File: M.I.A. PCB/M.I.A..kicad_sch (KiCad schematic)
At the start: 41 parts, among them J1 USB_C_Receptacle_USB2.0_16P, SW1 SW_Push, SW2 SW_Push, U1 W25Q128JVS, U2 RP2350B-QFN80, Y1 ABM8-272-T3

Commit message: Finished Layout other than gps, extra connectors, and ignition lines
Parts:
- C14, C15, C16, C3: footprint Capacitor_SMD:C_0603_1608Metric -> Capacitor_SMD:C_0805_2012Metric
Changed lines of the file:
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@@
 			)
 		)
-		(property "Footprint" "Capacitor_SMD:C_0603_1608Metric"
+		(property "Footprint" "Capacitor_SMD:C_0805_2012Metric"
 			(at 96.2152 22.86 0)
 			(effects
@@
 			)
 		)
-		(property "Footprint" "Capacitor_SMD:C_0603_1608Metric"
+		(property "Footprint" "Capacitor_SMD:C_0805_2012Metric"
 			(at 30.1752 46.99 0)
 			(effects
@@
 			)
 		)
-		(property "Footprint" "Capacitor_SMD:C_0603_1608Metric"
+		(property "Footprint" "Capacitor_SMD:C_0805_2012Metric"
 			(at 21.2852 46.99 0)
 			(effects
@@
 			)
 		)
-		(property "Footprint" "Capacitor_SMD:C_0603_1608Metric"
+		(property "Footprint" "Capacitor_SMD:C_0805_2012Metric"
 			(at 50.4952 30.48 0)
 			(effects

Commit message: Worked More on Layout/Wiring
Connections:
- net PWM1: now also U2.57 (GPIO46_ADC6)
- net PWM2: now also U2.58 (GPIO47_ADC7)
- net PWM3: now also U2.56 (GPIO45_ADC5)
- net PWM4: now also U2.55 (GPIO44_ADC4)
- net PWM5: now also U2.54 (GPIO43_ADC3)
- net PWM6: now also U2.53 (GPIO42_ADC2)
- net PWM7: now also U2.52 (GPIO41_ADC1)
- net PWM8: now also U2.49 (GPIO40_ADC0)
- net SD_ChipDetect: now also U2.44 (GPIO35)
- net SD_ChipSelect: now also U2.46 (GPIO37)
- net SPI_MISO_SD: now also U2.45 (GPIO36)
- net SPI_MOSI_SD: now also U2.48 (GPIO39)
- net SPI_SCK_SD: now also U2.47 (GPIO38)
- net IGN_4: now reaches U2.39 (GPIO31)
- net IGN_3: now reaches U2.40 (GPIO32)
- net IGN_2: now reaches U2.42 (GPIO33)
- net IGN_1: now reaches U2.43 (GPIO34)

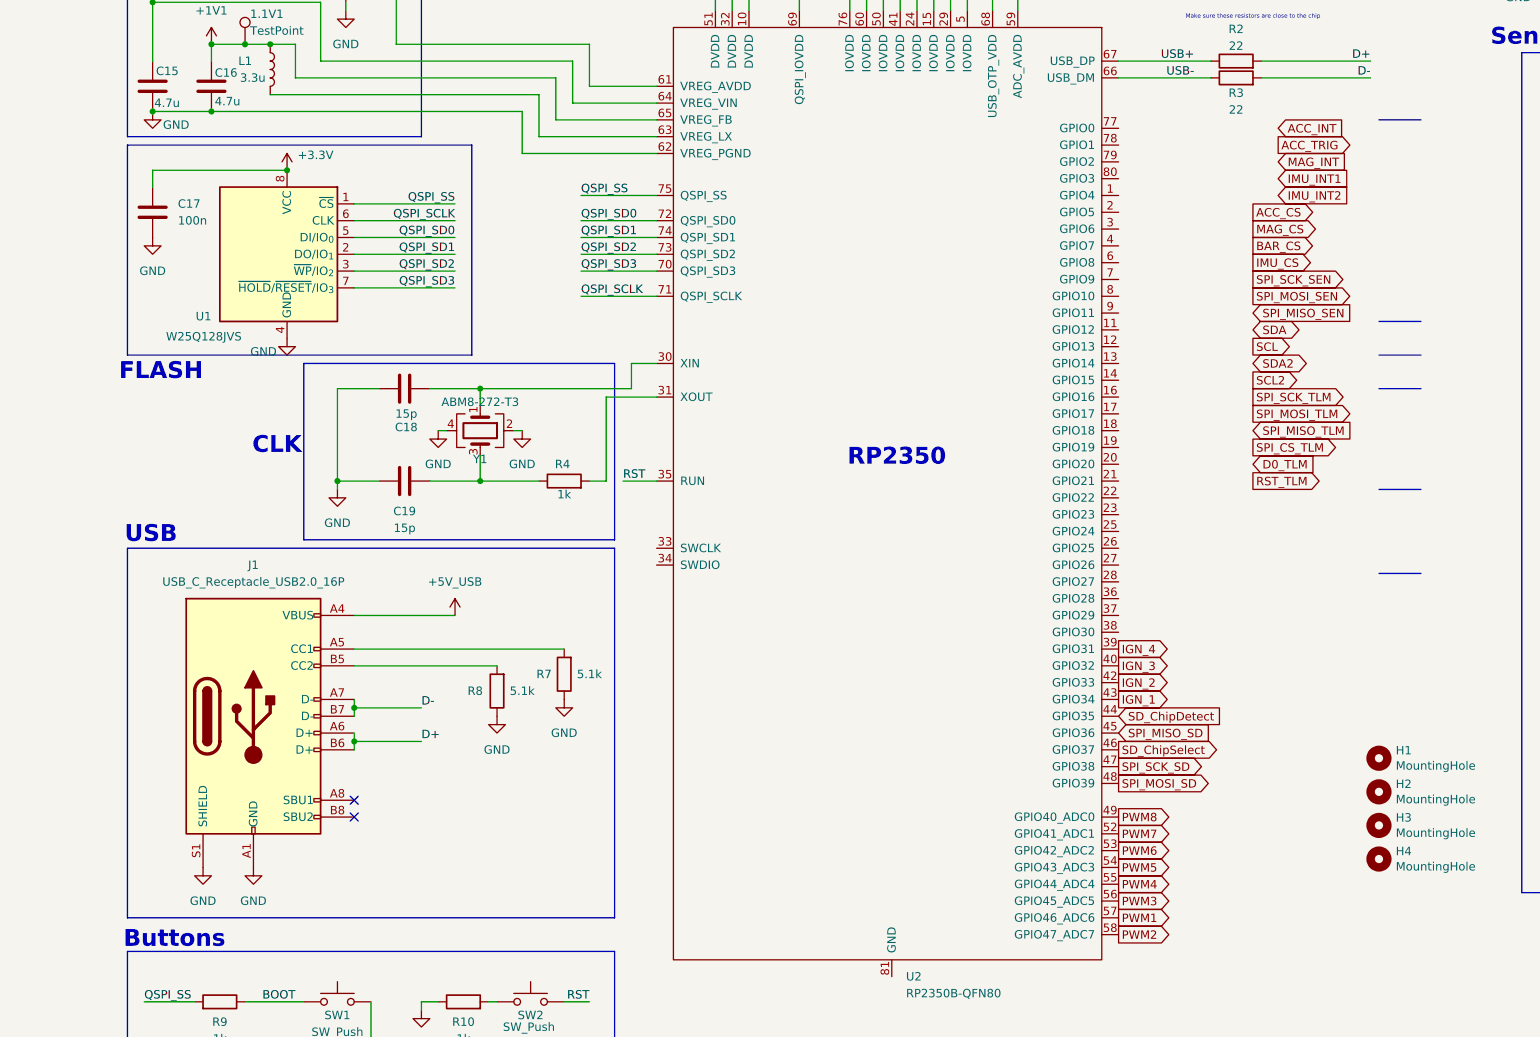
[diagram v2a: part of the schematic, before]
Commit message: Wired Sensors
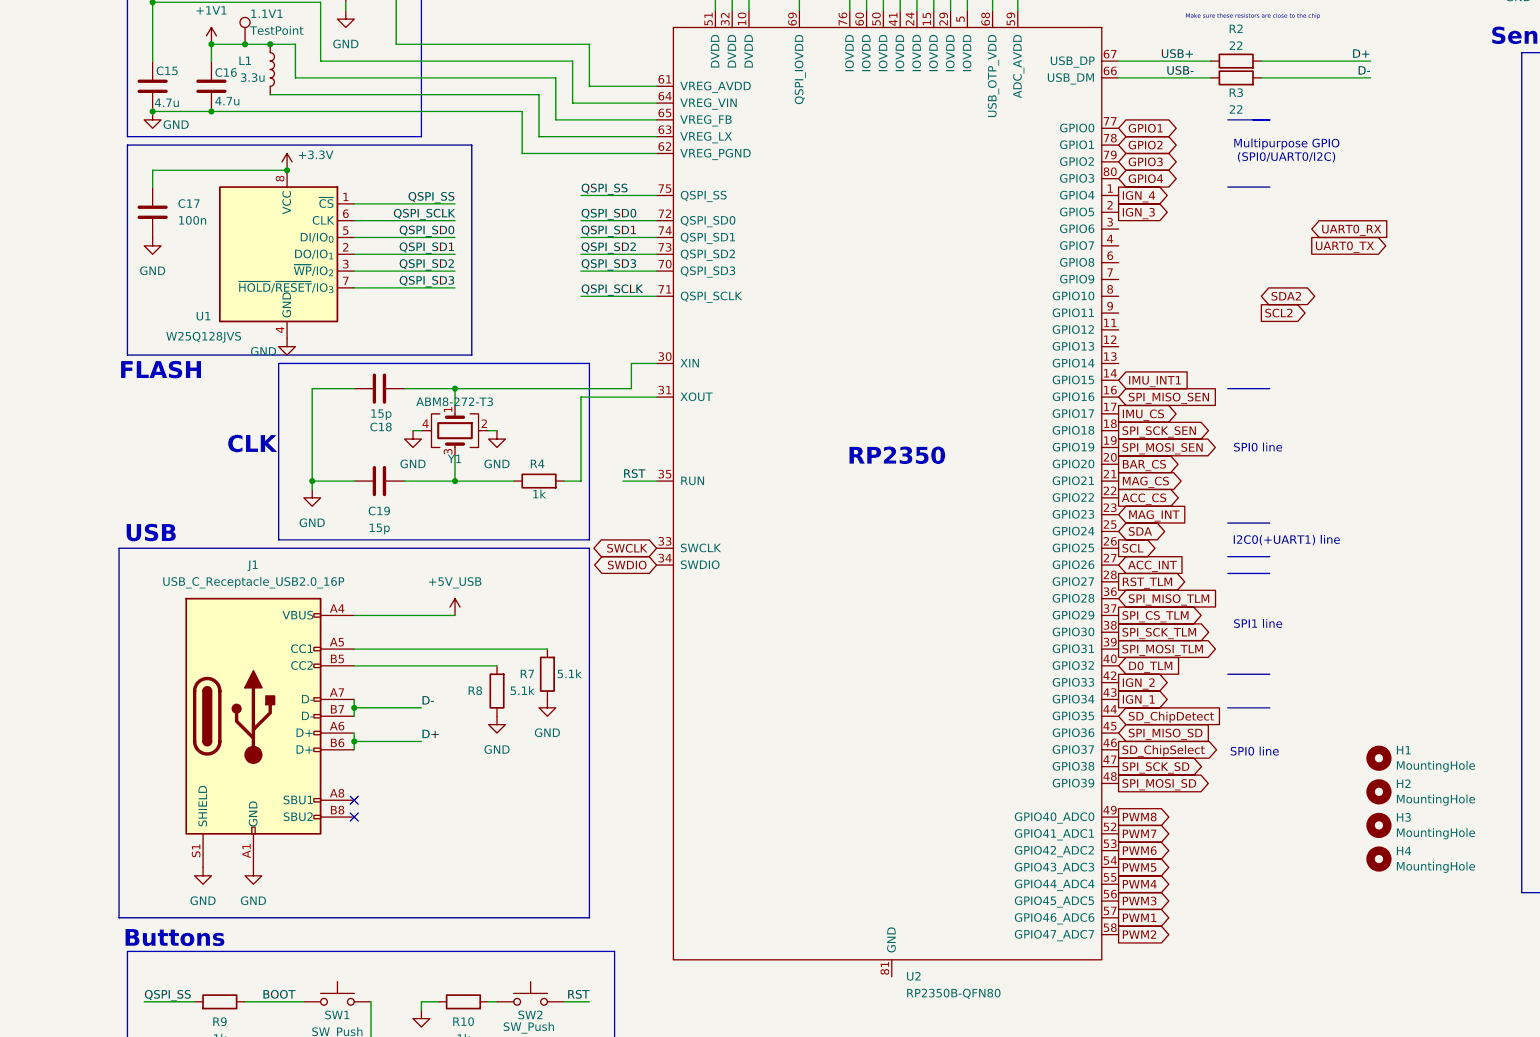
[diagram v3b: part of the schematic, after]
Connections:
- net ACC_CS: now also U2.22 (GPIO22)
- net ACC_INT: now also U2.27 (GPIO26)
- net BAR_CS: now also U2.20 (GPIO20)
- net D0_TLM: now also U2.40 (GPIO32)
- net IGN_3: now also U2.2 (GPIO5); no longer U2.40 (GPIO32)
- net IGN_4: now also U2.1 (GPIO4); no longer U2.39 (GPIO31)
- net IMU_CS: now also U2.17 (GPIO17)
- net IMU_INT1: now also U2.14 (GPIO15)
- net MAG_CS: now also U2.21 (GPIO21)
- net MAG_INT: now also U2.23 (GPIO23)
- net RST_TLM: now also U2.28 (GPIO27)
- net SCL: now also U2.26 (GPIO25)
- net SDA: now also U2.25 (GPIO24)
- net SPI_CS_TLM: now also U2.37 (GPIO29)
- net SPI_MISO_SEN: now also U2.16 (GPIO16)
- net SPI_MISO_TLM: now also U2.36 (GPIO28)
- net SPI_MOSI_SEN: now also U2.19 (GPIO19)
- net SPI_MOSI_TLM: now also U2.39 (GPIO31)
- net SPI_SCK_SEN: now also U2.18 (GPIO18)
- net SPI_SCK_TLM: now also U2.38 (GPIO30)
- net SWCLK: now reaches U2.33 (SWCLK)
- net SWDIO: now reaches U2.34 (SWDIO)
- net GPIO1: now reaches U2.77 (GPIO0)
- net GPIO2: now reaches U2.78 (GPIO1)
- net GPIO3: now reaches U2.79 (GPIO2)
- net GPIO4: now reaches U2.80 (GPIO3)
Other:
- note added: "I2C0(+UART1) line"
- note added: "Multipurpose GPIO (SPI0/UART0/I2C)"
- note added: "SPI0 line"
- note added: "SPI1 line"
- moved on the sheet: C18, C19, R4, R7, Y1

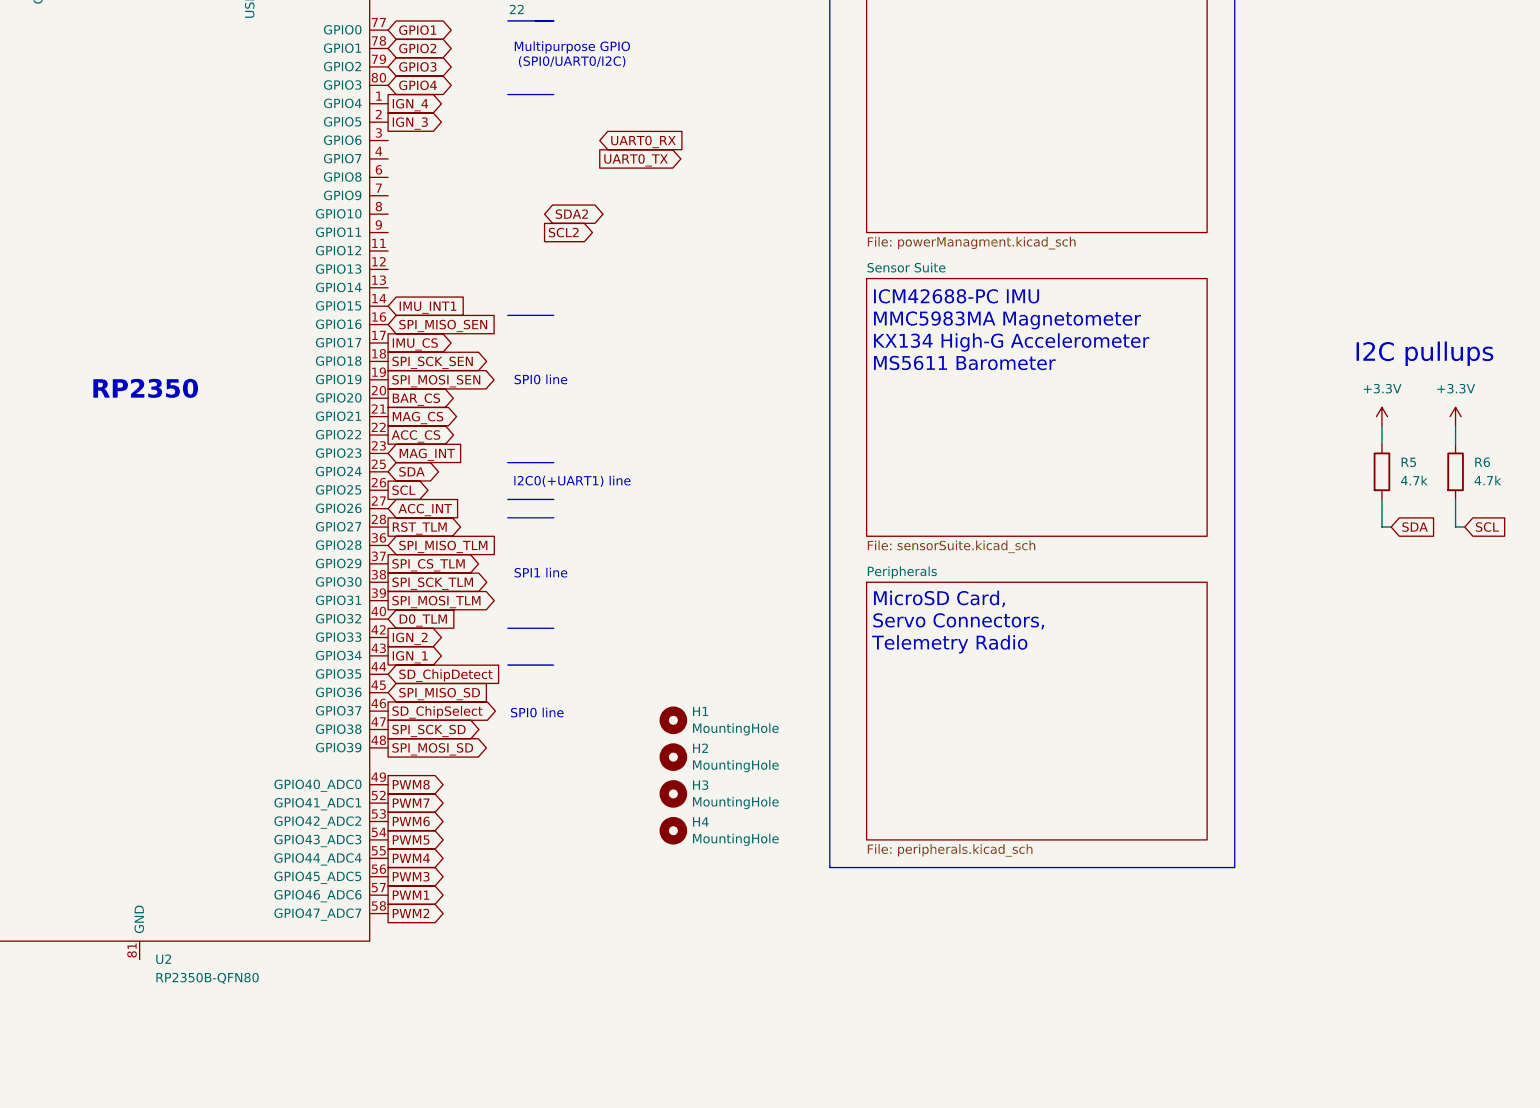
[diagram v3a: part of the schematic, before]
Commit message: routed continuity sensing and pwm routing fixed
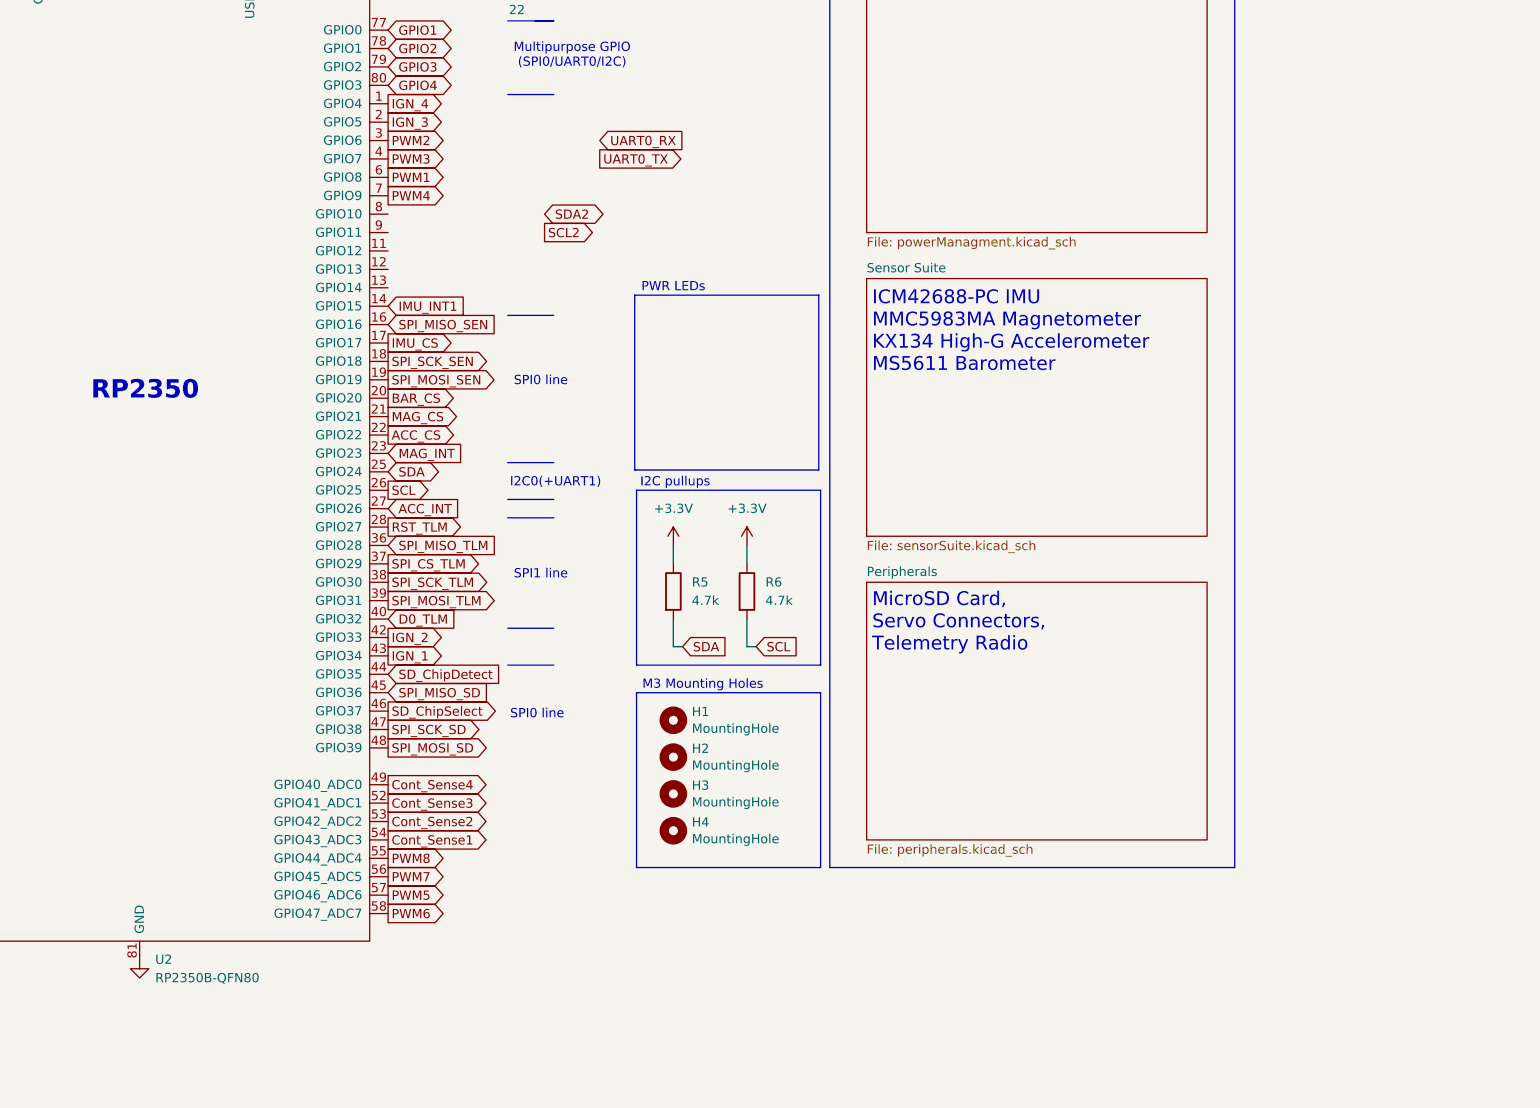
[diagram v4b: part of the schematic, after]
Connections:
- net GND: now also U2.81 (GND)
- net PWM1: now also U2.6 (GPIO8); no longer U2.57 (GPIO46_ADC6)
- net PWM2: now also U2.3 (GPIO6); no longer U2.58 (GPIO47_ADC7)
- net PWM3: now also U2.4 (GPIO7); no longer U2.56 (GPIO45_ADC5)
- net PWM4: now also U2.7 (GPIO9); no longer U2.55 (GPIO44_ADC4)
- net PWM5: now also U2.57 (GPIO46_ADC6); no longer U2.54 (GPIO43_ADC3)
- net PWM6: now also U2.58 (GPIO47_ADC7); no longer U2.53 (GPIO42_ADC2)
- net PWM7: now also U2.56 (GPIO45_ADC5); no longer U2.52 (GPIO41_ADC1)
- net PWM8: now also U2.55 (GPIO44_ADC4); no longer U2.49 (GPIO40_ADC0)
- new net Cont_Sense1: U2.54 (GPIO43_ADC3)
- new net Cont_Sense2: U2.53 (GPIO42_ADC2)
- new net Cont_Sense3: U2.52 (GPIO41_ADC1)
- new net Cont_Sense4: U2.49 (GPIO40_ADC0)
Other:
- note added: "I2C0(+UART1)"
- note added: "M3 Mounting Holes"
- note added: "PWR LEDs"
- note removed: "I2C0(+UART1) line"
- moved on the sheet: R5, R6
